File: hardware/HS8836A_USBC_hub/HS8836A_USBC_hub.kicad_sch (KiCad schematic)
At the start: 18 parts, among them J1 USB_C_Receptacle_USB2.0, J2 USB_A, J3 USB_A, J4 USB_A, J5 USB_A, J6 USB_B_Micro, U1 HS8836A

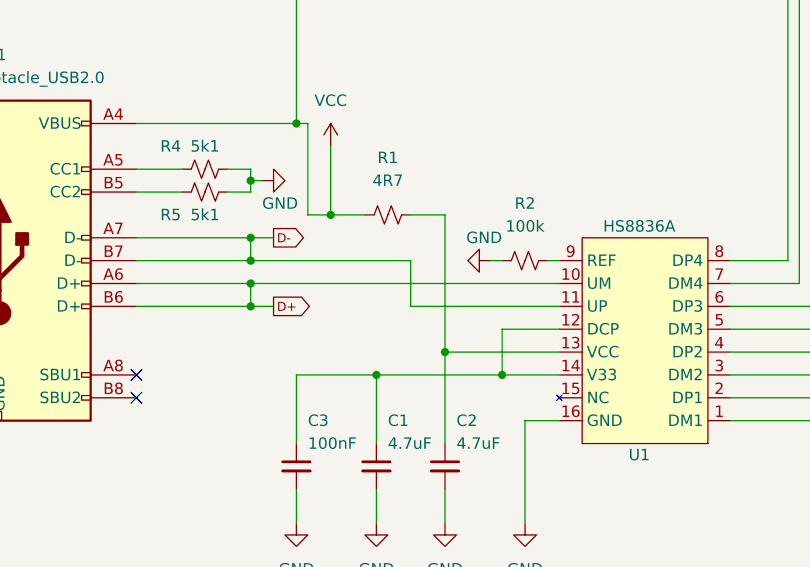
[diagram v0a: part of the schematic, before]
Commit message: swapped dp and dm lines on the controller
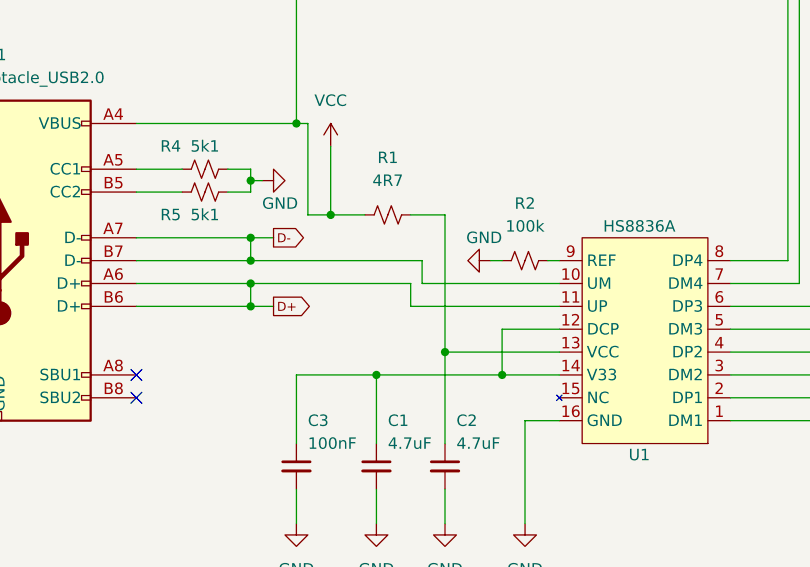
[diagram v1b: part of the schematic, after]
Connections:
- net D+: now also U1.11 (UP); no longer U1.10 (UM)
- net D-: now also U1.10 (UM); no longer U1.11 (UP)
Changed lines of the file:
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@@
   (junction (at 95.25 77.47) (diameter 0) (color 0 0 0 0)
   )
+  (junction (at 95.25 66.04) (diameter 0) (color 0 0 0 0)
+  )
+  (junction (at 116.84 85.09) (diameter 0) (color 0 0 0 0)
+  )
+  (junction (at 109.22 87.63) (diameter 0) (color 0 0 0 0)
+  )
+  (junction (at 64.77 43.18) (diameter 0) (color 0 0 0 0)
+  )
+  (junction (at 236.22 48.26) (diameter 0) (color 0 0 0 0)
+  )
+  (junction (at 95.25 80.01) (diameter 0) (color 0 0 0 0)
+  )
+  (junction (at 95.25 72.39) (diameter 0) (color 0 0 0 0)
+  )
+  (junction (at 236.22 151.13) (diameter 0) (color 0 0 0 0)
+  )
+  (junction (at 59.69 100.33) (diameter 0) (color 0 0 0 0)
+  )
+  (junction (at 123.19 87.63) (diameter 0) (color 0 0 0 0)
+  )
+  (junction (at 100.33 59.69) (diameter 0) (color 0 0 0 0)
+  )
+  (junction (at 236.22 116.84) (diameter 0) (color 0 0 0 0)
+  )
+  (junction (at 236.22 82.55) (diameter 0) (color 0 0 0 0)
+  )
+  (junction (at 104.14 69.85) (diameter 0) (color 0 0 0 0)
+  )
   (junction (at 95.25 74.93) (diameter 0) (color 0 0 0 0)
-  )
-  (junction (at 95.25 66.04) (diameter 0) (color 0 0 0 0)
-  )
-  (junction (at 116.84 85.09) (diameter 0) (color 0 0 0 0)
-  )
-  (junction (at 109.22 87.63) (diameter 0) (color 0 0 0 0)
-  )
-  (junction (at 64.77 43.18) (diameter 0) (color 0 0 0 0)
-  )
-  (junction (at 236.22 48.26) (diameter 0) (color 0 0 0 0)
-  )
-  (junction (at 95.25 80.01) (diameter 0) (color 0 0 0 0)
-  )
-  (junction (at 95.25 72.39) (diameter 0) (color 0 0 0 0)
-  )
-  (junction (at 236.22 151.13) (diameter 0) (color 0 0 0 0)
-  )
-  (junction (at 59.69 100.33) (diameter 0) (color 0 0 0 0)
-  )
-  (junction (at 123.19 87.63) (diameter 0) (color 0 0 0 0)
-  )
-  (junction (at 100.33 59.69) (diameter 0) (color 0 0 0 0)
-  )
-  (junction (at 236.22 116.84) (diameter 0) (color 0 0 0 0)
-  )
-  (junction (at 236.22 82.55) (diameter 0) (color 0 0 0 0)
-  )
-  (junction (at 104.14 69.85) (diameter 0) (color 0 0 0 0)
   )
   (no_connect (at 82.55 90.17))
@@
     (stroke (width 0) (type default))
   )
+  (wire (pts (xy 114.3 77.47) (xy 129.54 77.47))
+    (stroke (width 0) (type default))
+  )
   (wire (pts (xy 156.21 77.47) (xy 156.21 38.1))
     (stroke (width 0) (type default))
@@
     (stroke (width 0) (type default))
   )
-  (wire (pts (xy 113.03 74.93) (xy 113.03 80.01))
-    (stroke (width 0) (type default))
-  )
   (wire (pts (xy 233.68 114.3) (xy 233.68 116.84))
     (stroke (width 0) (type default))
@@
     (stroke (width 0) (type default))
   )
-  (wire (pts (xy 95.25 74.93) (xy 113.03 74.93))
-    (stroke (width 0) (type default))
-  )
-  (wire (pts (xy 95.25 77.47) (xy 129.54 77.47))
+  (wire (pts (xy 114.3 74.93) (xy 114.3 77.47))
     (stroke (width 0) (type default))
   )
@@
     (stroke (width 0) (type default))
   )
+  (wire (pts (xy 95.25 77.47) (xy 113.03 77.47))
+    (stroke (width 0) (type default))
+  )
   (wire (pts (xy 101.6 69.85) (xy 104.14 69.85))
     (stroke (width 0) (type default))
@@
     (stroke (width 0) (type default))
   )
+  (wire (pts (xy 113.03 77.47) (xy 113.03 80.01))
+    (stroke (width 0) (type default))
+  )
   (wire (pts (xy 236.22 148.59) (xy 236.22 151.13))
     (stroke (width 0) (type default))
@@
     (stroke (width 0) (type default))
   )
+  (wire (pts (xy 95.25 74.93) (xy 114.3 74.93))
+    (stroke (width 0) (type default))
+  )

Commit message: Updated Gerbers and images
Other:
- title: (none) -> HS8836A USB-C Hub
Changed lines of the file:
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@@
 (kicad_sch (version 20230121) (generator eeschema)
   (paper "A4")
+  (title_block
+    (title "HS8836A USB-C Hub")
+    (date "2024-04-13")
+    (rev "2.0")
+  )
   (junction (at 95.25 77.47) (diameter 0) (color 0 0 0 0)
   )
